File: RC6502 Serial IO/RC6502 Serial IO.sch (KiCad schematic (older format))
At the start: 16 parts, among them J1 CONN_01X39, J2 Arduino_Nano_Header, J3 SPI Breakout, SW1 Reset, U1 74HCT04, U2 WD65C21, U3 74LS138, U4 MCP23S17

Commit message: Mapped out PCB
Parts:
- C4: value CP1 -> 10nF; footprint (none) -> Capacitors_THT:C_Disc_D4.7mm_W2.5mm_P5.00mm
- J2: footprint (none) -> Modules:Arduino_Nano
- J3: footprint (none) -> Pin_Headers:Pin_Header_Straight_1x05_Pitch2.54mm
- JP1: footprint (none) -> Pin_Headers:Pin_Header_Angled_1x02_Pitch2.54mm
- R1, R2, R3: footprint (none) -> Resistors_THT:R_Axial_DIN0207_L6.3mm_D2.5mm_P10.16mm_Horizontal
- SW1: footprint (none) -> Buttons_Switches_THT:SW_PUSH_6mm
- U1: footprint (none) -> Housings_DIP:DIP-14_W7.62mm_Socket
- U2: footprint (none) -> Housings_DIP:DIP-40_W15.24mm_Socket
- U3: footprint (none) -> Housings_DIP:DIP-16_W7.62mm_Socket
- U4: footprint (none) -> Housings_DIP:DIP-28_W7.62mm_Socket
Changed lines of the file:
@@
 F 0 "U2" H 3300 700 60  0000 C CNN
 F 1 "WD65C21" V 3300 1750 60  0000 C CNN
-F 2 "" H 2800 2050 60  0000 C CNN
+F 2 "Housings_DIP:DIP-40_W15.24mm_Socket" H 2800 2050 60  0001 C CNN
 F 3 "" H 2800 2050 60  0000 C CNN
 	1    3300 1850
@@
 F 0 "U3" H 3400 4300 50  0000 C CNN
 F 1 "74LS138" H 3450 3251 50  0000 C CNN
-F 2 "" H 3300 3800 50  0001 C CNN
+F 2 "Housings_DIP:DIP-16_W7.62mm_Socket" H 3300 3800 50  0001 C CNN
 F 3 "" H 3300 3800 50  0001 C CNN
 	1    3300 3800
@@
 F 0 "U1" H 2000 2850 50  0000 C CNN
 F 1 "74HCT04" H 2050 2650 50  0000 C CNN
-F 2 "" H 1850 2750 50  0001 C CNN
+F 2 "Housings_DIP:DIP-14_W7.62mm_Socket" H 1850 2750 50  0001 C CNN
 F 3 "" H 1850 2750 50  0001 C CNN
 	1    1850 2750
@@
 P 1250 2750
 F 0 "C4" H 1275 2850 50  0000 L CNN
-F 1 "CP1" H 1275 2650 50  0000 L CNN
-F 2 "" H 1250 2750 50  0001 C CNN
+F 1 "10nF" H 1275 2650 50  0000 L CNN
+F 2 "Capacitors_THT:C_Disc_D4.7mm_W2.5mm_P5.00mm" H 1250 2750 50  0001 C CNN
 F 3 "" H 1250 2750 50  0001 C CNN
 	1    1250 2750
@@
 F 0 "U4" H 5600 2825 50  0000 R CNN
 F 1 "MCP23S17" H 5600 2750 50  0000 R CNN
-F 2 "" H 5750 850 50  0001 L CNN
+F 2 "Housings_DIP:DIP-28_W7.62mm_Socket" H 5750 850 50  0001 L CNN
 F 3 "" H 5950 2800 50  0001 C CNN
 	1    5700 1800
@@
 F 0 "J2" H 7750 2500 60  0000 C CNN
 F 1 "Arduino_Nano_Header" H 7750 900 60  0000 C CNN
-F 2 "" H 7750 1700 60  0000 C CNN
+F 2 "Modules:Arduino_Nano" H 7750 1700 60  0001 C CNN
 F 3 "" H 7750 1700 60  0000 C CNN
 	1    7750 1700
@@
 F 0 "R3" V 7830 3250 50  0000 C CNN
 F 1 "10k" V 7750 3250 50  0000 C CNN
-F 2 "" V 7680 3250 50  0001 C CNN
+F 2 "Resistors_THT:R_Axial_DIN0207_L6.3mm_D2.5mm_P10.16mm_Horizontal" V 7680 3250 50  0001 C CNN
 F 3 "" H 7750 3250 50  0001 C CNN
 	1    7750 3250
@@
 F 0 "SW1" H 8850 1300 50  0000 L CNN
 F 1 "Reset" H 8800 1140 50  0000 C CNN
-F 2 "" H 8800 1400 50  0001 C CNN
+F 2 "Buttons_Switches_THT:SW_PUSH_6mm" H 8800 1400 50  0001 C CNN
 F 3 "" H 8800 1400 50  0001 C CNN
 	1    8800 1200
@@
 F 0 "JP1" H 8700 1530 50  0000 C CNN
 F 1 "USB Power" H 8710 1390 50  0000 C CNN
-F 2 "" H 8700 1450 50  0001 C CNN
+F 2 "Pin_Headers:Pin_Header_Angled_1x02_Pitch2.54mm" H 8700 1450 50  0001 C CNN
 F 3 "" H 8700 1450 50  0001 C CNN
 	1    8700 1450
@@
 F 0 "R2" V 7830 3050 50  0000 C CNN
 F 1 "10k" V 7750 3050 50  0000 C CNN
-F 2 "" V 7680 3050 50  0001 C CNN
+F 2 "Resistors_THT:R_Axial_DIN0207_L6.3mm_D2.5mm_P10.16mm_Horizontal" V 7680 3050 50  0001 C CNN
 F 3 "" H 7750 3050 50  0001 C CNN
 	1    7750 3050
@@
 F 0 "R1" V 7830 2850 50  0000 C CNN
 F 1 "10k" V 7750 2850 50  0000 C CNN
-F 2 "" V 7680 2850 50  0001 C CNN
+F 2 "Resistors_THT:R_Axial_DIN0207_L6.3mm_D2.5mm_P10.16mm_Horizontal" V 7680 2850 50  0001 C CNN
 F 3 "" H 7750 2850 50  0001 C CNN
 	1    7750 2850
@@
 F 0 "J3" H 7750 4100 50  0000 C CNN
 F 1 "SPI Breakout" V 7850 3800 50  0000 C CNN
-F 2 "" H 7750 3800 50  0001 C CNN
+F 2 "Pin_Headers:Pin_Header_Straight_1x05_Pitch2.54mm" H 7750 3800 50  0001 C CNN
 F 3 "" H 7750 3800 50  0001 C CNN
 	1    7750 3800

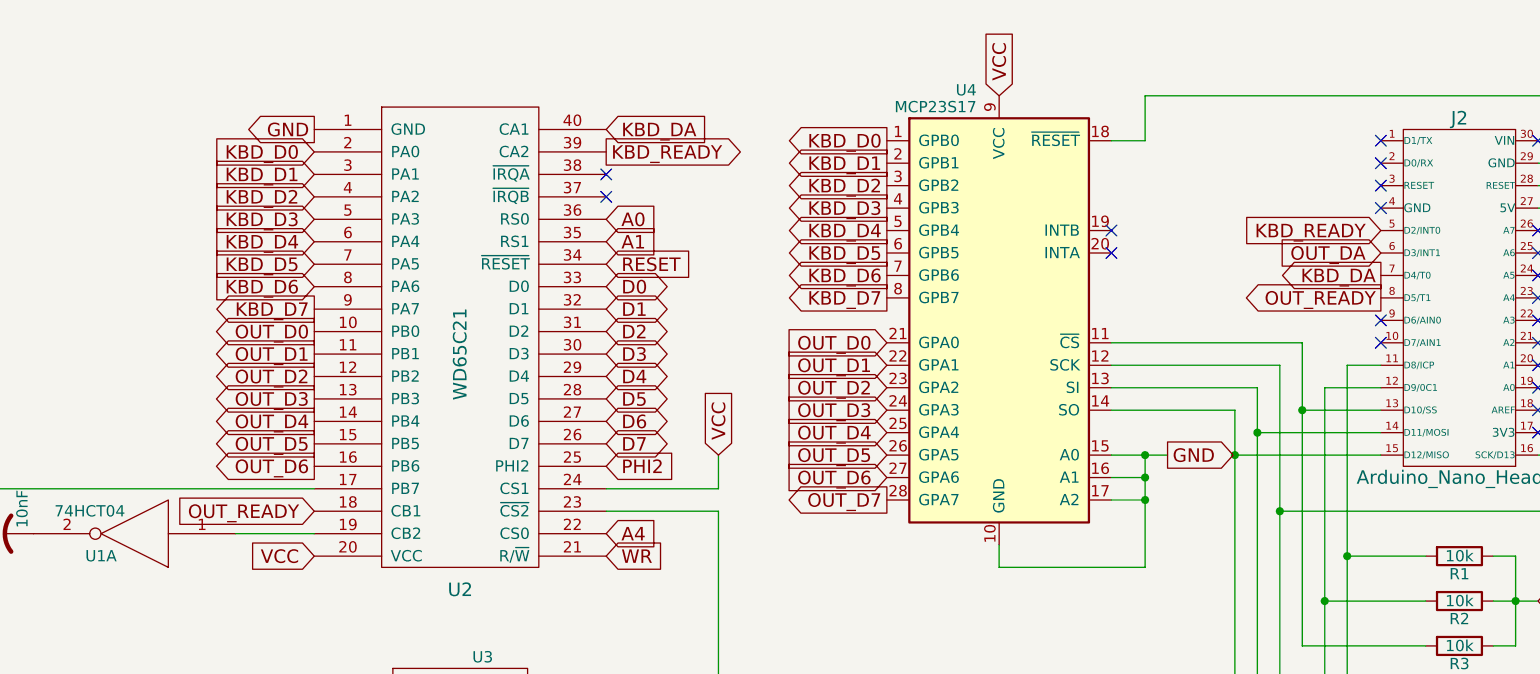
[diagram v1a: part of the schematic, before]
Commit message: Non-functional version of serial communications
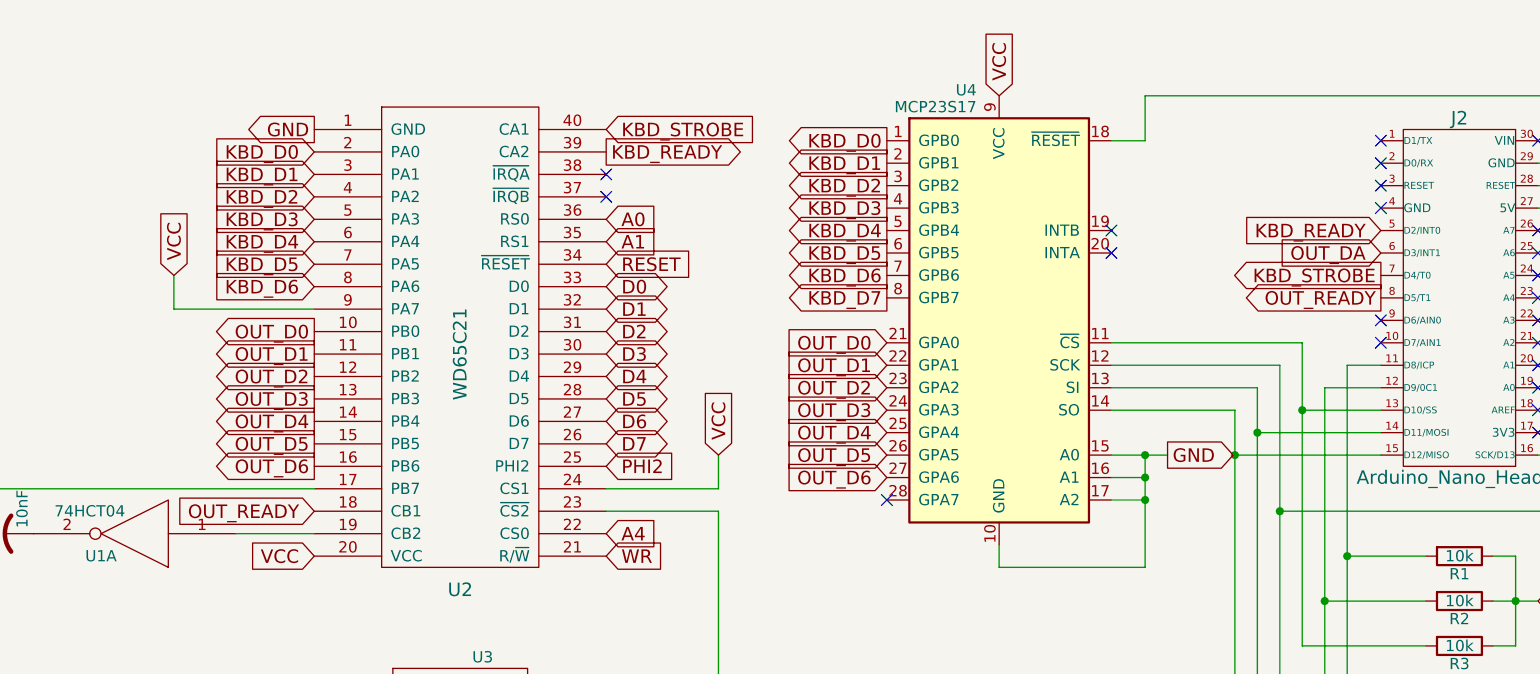
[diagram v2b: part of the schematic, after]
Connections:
- net KBD_D7: no longer U2.9 (PA7)
- net VCC: now also U2.9 (PA7)
- net KBD_DA renamed KBD_STROBE
- net OUT_D7: no longer names the net of U4.28 (GPA7)
- no-connect marks 48 -> 49
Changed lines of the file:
@@
 VCC
 Text GLabel 3950 950  2    60   Input ~ 0
-KBD_DA
+KBD_STROBE
 Text GLabel 3950 1050 2    60   Output ~ 0
 KBD_READY
@@
 	1    0    0    -1
 $EndComp
-Text GLabel 2650 1750 0    60   Output ~ 0
-KBD_D7
 Text GLabel 5200 1900 0    60   Input ~ 0
 OUT_D0
@@
 Wire Wire Line
 	8350 1300 8100 1300
-Text GLabel 5200 2600 0    60   Output ~ 0
-OUT_D7
 Text GLabel 7400 1400 0    60   Input ~ 0
 KBD_READY
 Text GLabel 7400 1600 0    60   Output ~ 0
-KBD_DA
+KBD_STROBE
 Text GLabel 7400 1700 0    60   Output ~ 0
 OUT_READY
@@
 NoConn ~ 7400 1000
 NoConn ~ 7400 1300
+NoConn ~ 5200 2600
+Text GLabel 2025 1600 1    60   Input ~ 0
+VCC
+Wire Wire Line
+	2025 1600 2025 1750
+Wire Wire Line
+	2025 1750 2650 1750
 $EndSCHEMATC

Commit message: updated export
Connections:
- net KBD_D7: now also U2.9 (PA7)
- net VCC: no longer U2.9 (PA7)
- net OUT_READY renamed OUT_RDA
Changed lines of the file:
@@
 $EndComp
 Text GLabel 2650 2650 0    60   Input ~ 0
-OUT_READY
+OUT_RDA
 Text GLabel 950  2550 0    60   Output ~ 0
 OUT_DA
@@
 KBD_STROBE
 Text GLabel 7400 1700 0    60   Output ~ 0
-OUT_READY
+OUT_RDA
 Text GLabel 7400 1500 0    60   Input ~ 0
 OUT_DA
@@
 NoConn ~ 7400 1300
 NoConn ~ 5200 2600
-Text GLabel 2025 1600 1    60   Input ~ 0
-VCC
-Wire Wire Line
-	2025 1600 2025 1750
-Wire Wire Line
-	2025 1750 2650 1750
+Text GLabel 2650 1750 0    60   Input ~ 0
+KBD_D7
 $EndSCHEMATC

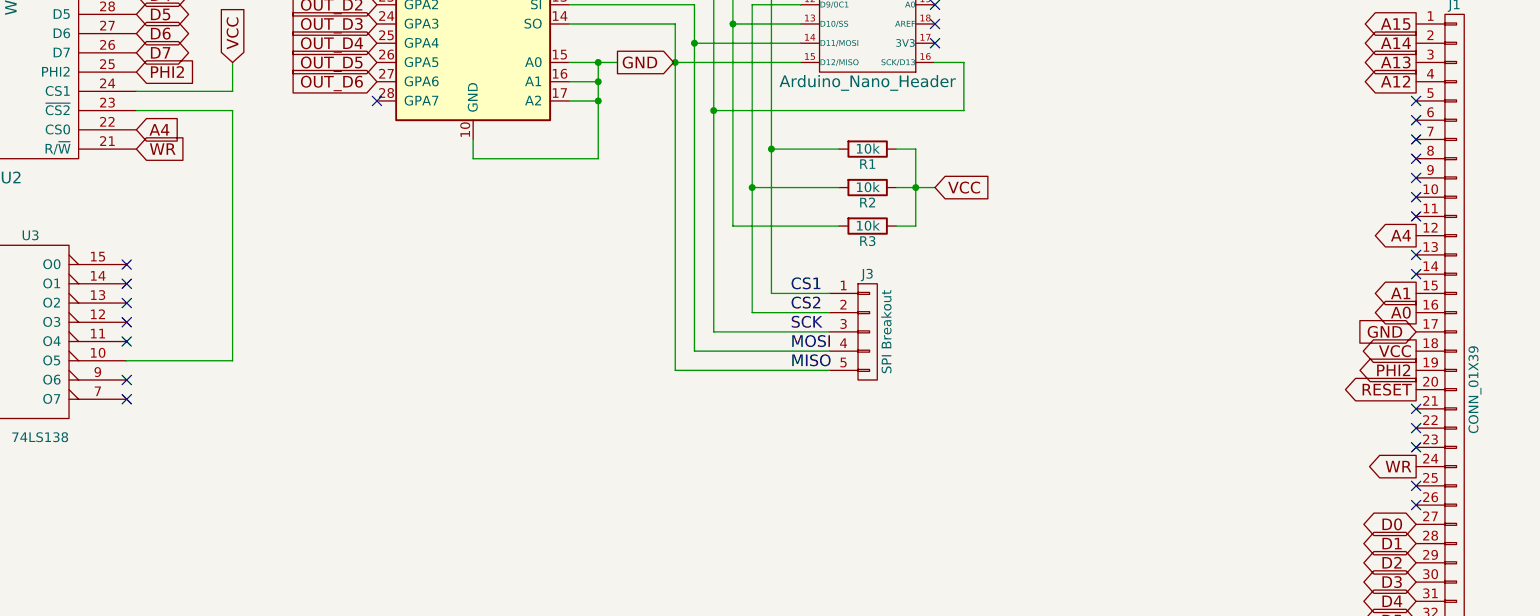
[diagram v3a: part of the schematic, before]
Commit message: Renamed some pins
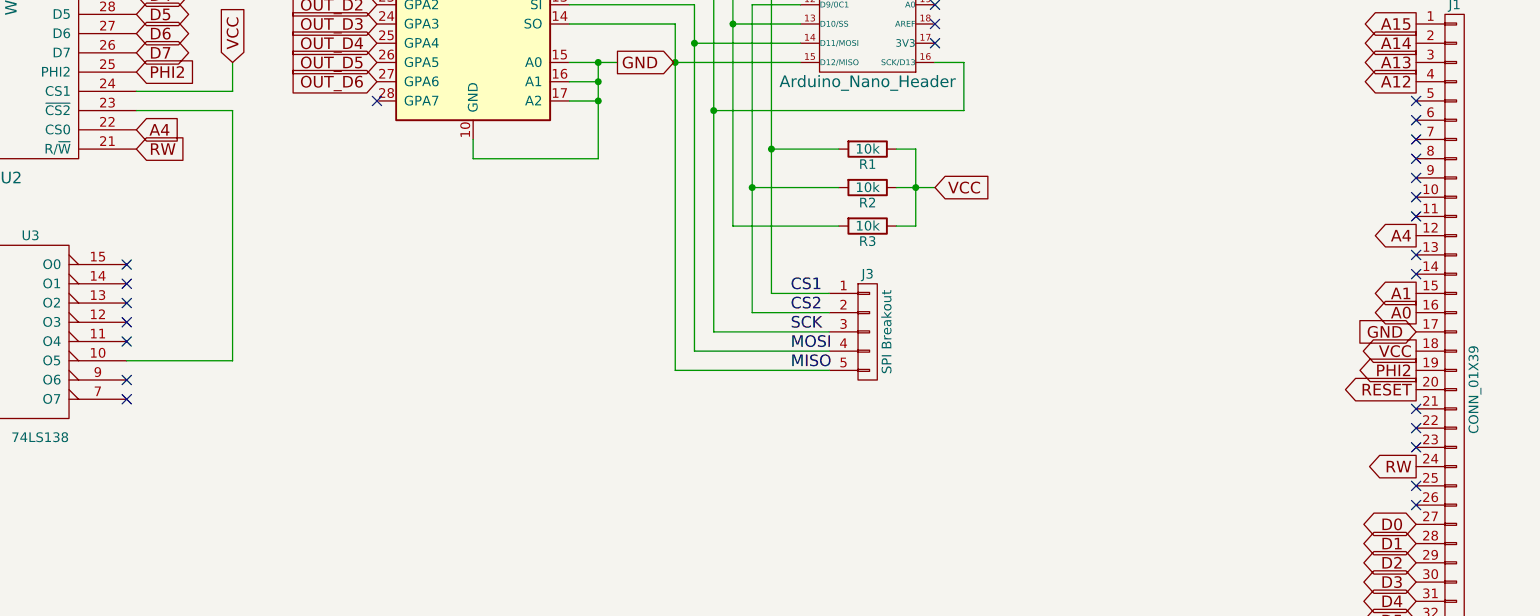
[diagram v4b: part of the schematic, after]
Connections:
- net WR renamed RW
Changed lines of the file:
@@
 $EndComp
 Text GLabel 10600 4500 0    60   Output ~ 0
-WR
+RW
 Text GLabel 3950 2850 2    60   Input ~ 0
-WR
+RW
 Text GLabel 2700 3550 0    60   Input ~ 0
 A13

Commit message: Serial IO Revision B
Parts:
- removed J3: SPI Breakout, Pin_Headers:Pin_Header_Straight_1x05_Pitch2.54mm, symbol CONN_01X05
- added C4: 100nF, Capacitors_THT:C_Disc_D4.7mm_W2.5mm_P5.00mm, symbol C
- added D1: 1N4848, Diodes_THT:D_DO-35_SOD27_P7.62mm_Horizontal, symbol D
- added J3: SPI Breakout, Pin_Headers:Pin_Header_Angled_1x06_Pitch2.54mm, symbol CONN_01X06
- added J4: Peripheral Bus, Connectors:IDC_Header_Straight_40pins, symbol CONN_02X20
- added R4, R5: 10k, Resistors_THT:R_Axial_DIN0207_L6.3mm_D2.5mm_P10.16mm_Horizontal, symbol R
- J2: value Arduino_Nano_Header -> Arduino Nano
- U3: value 74LS138 -> 74HCT38
- renumbered C4 to C5
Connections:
- net CS2 is gone; now on net CS1: J2.12 (D9/0C1), R2.2
- net CS1: now also J3.1 (P1); no longer J2.11 (D8/ICP), R1.2
- net GND: now also C4.2, J3.5 (P5), J4.19 (P19), J4.2 (P2), J4.22 (P22), J4.26 (P26), J4.30 (P30), J4.40 (P40)
- net KBD_D0: now also J4.35 (P35)
- net KBD_D1: now also J4.33 (P33)
- net KBD_D2: now also J4.31 (P31)
- net KBD_D3: now also J4.29 (P29)
- net KBD_D4: now also J4.27 (P27)
- net KBD_D5: now also J4.25 (P25)
- net KBD_D6: now also J4.23 (P23)
- net KBD_D7: now also J4.21 (P21)
- net KBD_READY: now also J4.37 (P37)
- net KBD_STROBE: now also J4.38 (P38)
- net MISO: now also J3.4 (P4)
- net MOSI: now also J3.3 (P3)
- net OUT_D0: now also J4.17 (P17)
- net OUT_D1: now also J4.15 (P15)
- net OUT_D2: now also J4.13 (P13)
- net OUT_D3: now also J4.11 (P11)
- net OUT_D4: now also J4.9 (P9)
- net OUT_D5: now also J4.7 (P7)
- net OUT_D6: now also J4.5 (P5)
- net OUT_DA: now also J4.3 (P3)
- net OUT_RDA: now also J4.34 (P34)
- net SCK: now also J3.2 (P2)
- net VCC: now also R1.2, C4.1, D1.1 (K), J3.6 (P6), R4.2, R5.2; no longer JP1.2, R1.1
- net TX: now reaches J1.35 (P35)
- net TX: now also J2.1 (D1/TX)
- net RX: now reaches J1.36 (P36)
- net RX: now also J2.2 (D0/RX)
- net P_RESET: now reaches J2.28 (RESET), SW1.1, U4.18 (~RESET)
- net P_RESET: now also J4.36 (P36), R5.1
- net KBD_DETECT: now reaches J2.10 (D7/AIN1)
- net KBD_DETECT: now also J4.39 (P39), R4.1
- net OUT_DETECT: now reaches J2.9 (D6/AIN0)
- net OUT_DETECT: now also R1.1, J4.32 (P32)
- new net: D1.2 (A), JP1.2
- no-connect marks 49 -> 55
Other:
- note added: "B"
- note removed: "A"
- moved on the sheet: C1, C2, C3, R2, R3, SW1

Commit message: Changed schematic symbol for capacitor on serial output line
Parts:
- C5: symbol CP1 -> C
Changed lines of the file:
@@
 $EndComp
 $Comp
-L CP1 C5
+L C C5
 U 1 1 590F85AC
 P 1250 2750
